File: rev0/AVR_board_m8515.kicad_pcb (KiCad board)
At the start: 2 copper layers, 16 parts, among them IC1 ATMEGA8515-A, IC2 ATMEGA8515-M, K1 SERIAL, P2 LEFT_HEADER, P3 CONN_3X2, P4 RIGHT_HEADER, SW1 SW_PUSH, X1 CRYSTAL_TH, X2 CRYSTAL_SMD

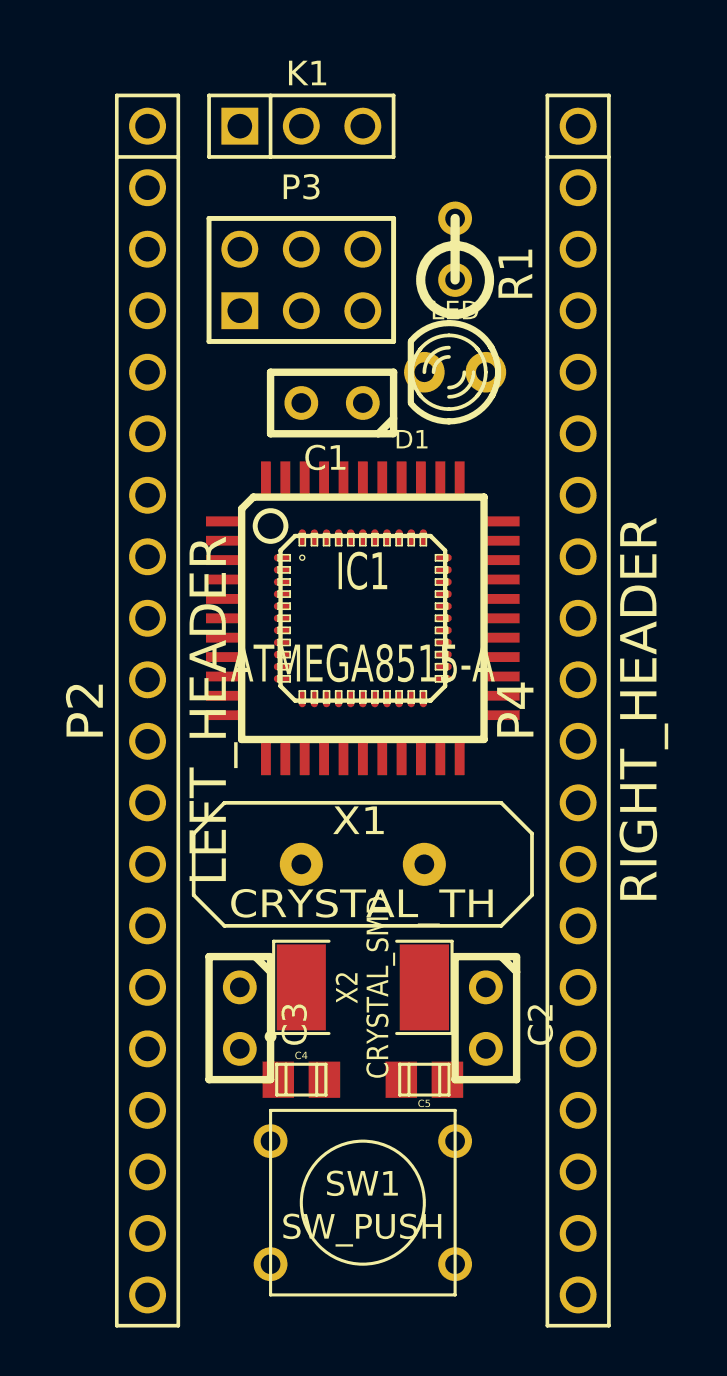
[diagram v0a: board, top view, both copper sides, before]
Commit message: added logo mod file, also added silkscreen refs
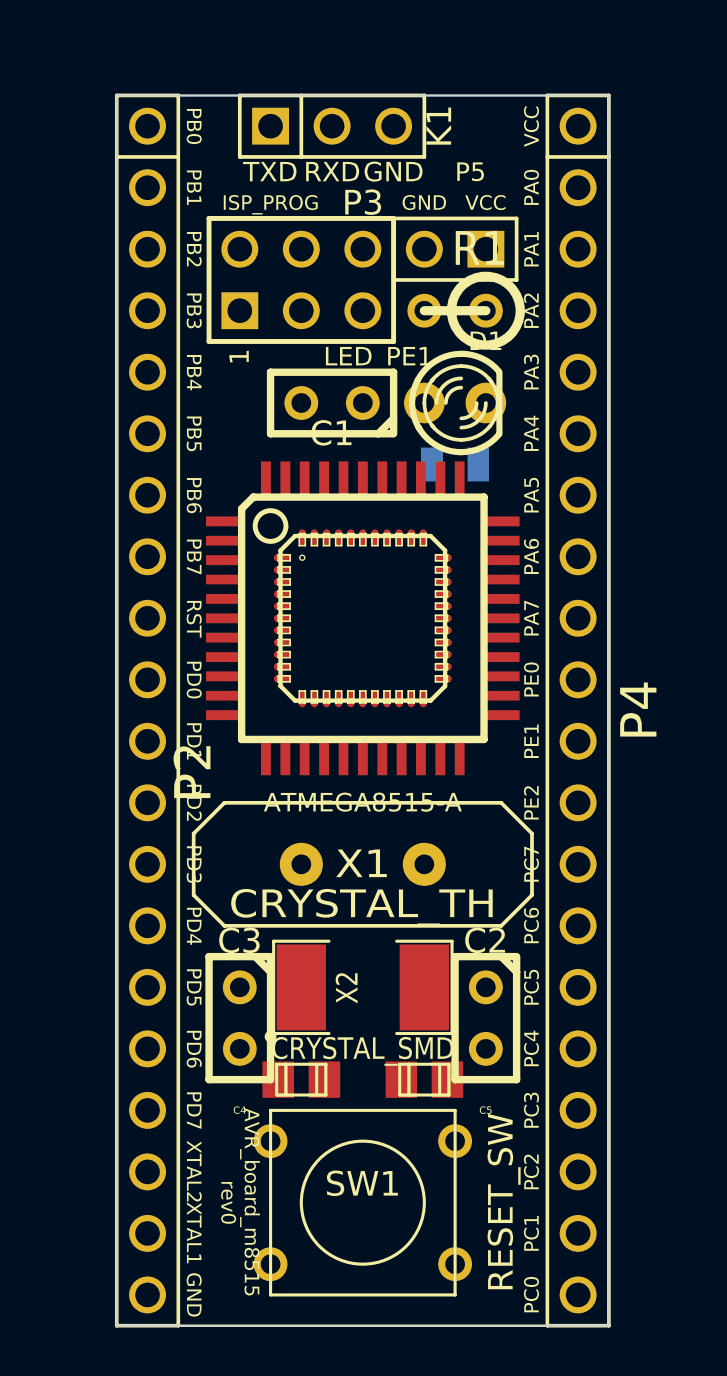
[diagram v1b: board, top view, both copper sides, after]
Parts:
- added G***: LOGO, LOGO, B.Cu at (146.1, 90.2)
- added JP1: LED_JUMPER, SM0805, B.Cu at (149.9, 83.8)
- added P5: EXT_PWR, PIN_ARRAY_2X1, F.Cu at (149.9, 74.9)
- D1: value LED -> LED_PE1
- SW1: value SW_PUSH -> RESET_SW
- moved R1 2.54 mm to (149.9, 77.5), turned to 180 degrees
- moved K1 1.27 mm to (144.8, 69.8)
- moved D1 1.27 mm to (149.9, 81.3), turned to 0 degrees
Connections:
- D1 pad 1: PE1 -> N-0000044
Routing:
- added copper zone on B.Cu, net GND
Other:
- board outline added: 20.3 x 50.8 mm
- board text added: "1"
- board text added: "AVR_board_m8515 rev0"
- board text added: "GND"
- board text added: "ISP_PROG"
- board text added: "PA0"
- board text added: "PA1"
- board text added: "PA2"
- board text added: "PA3"
- board text added: "PA4"
- board text added: "PA5"
- board text added: "PA6"
- board text added: "PA7"
- board text added: "PB0"
- board text added: "PB1"
- board text added: "PB2"
- board text added: "PB3"
- board text added: "PB4"
- board text added: "PB5"
- board text added: "PB6"
- board text added: "PB7"
- board text added: "PC0"
- board text added: "PC1"
- board text added: "PC2"
- board text added: "PC3"
- board text added: "PC4"
- board text added: "PC5"
- board text added: "PC6"
- board text added: "PC7"
- board text added: "PD0"
- board text added: "PD1"
- board text added: "PD2"
- board text added: "PD3"
- board text added: "PD4"
- board text added: "PD5"
- board text added: "PD6"
- board text added: "PD7"
- board text added: "PE0"
- board text added: "PE1"
- board text added: "PE2"
- board text added: "RST"
- board text added: "RXD"
- board text added: "TXD"
- board text added: "VCC"
- board text added: "XTAL1"
- board text added: "XTAL2"

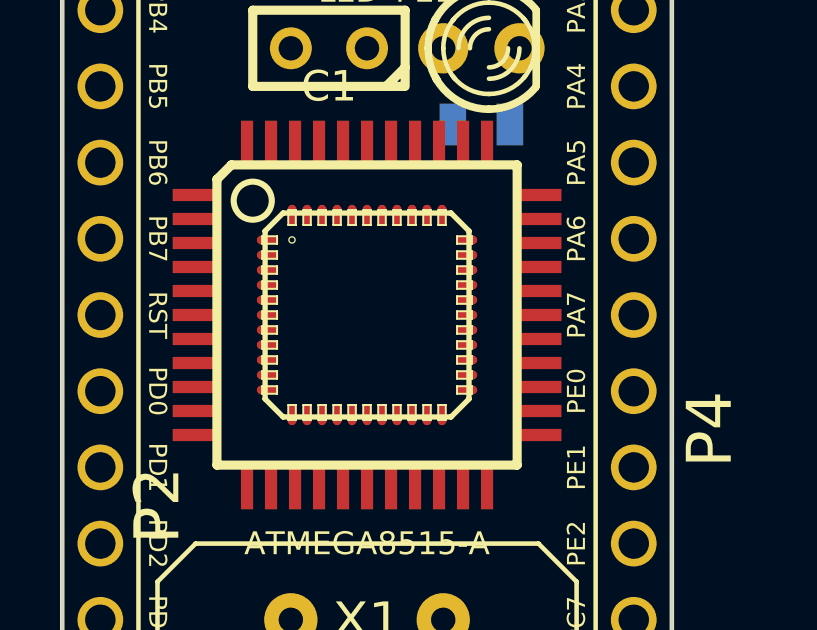
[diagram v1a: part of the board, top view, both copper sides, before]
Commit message: removed the mlf44 footprint due to routing issues
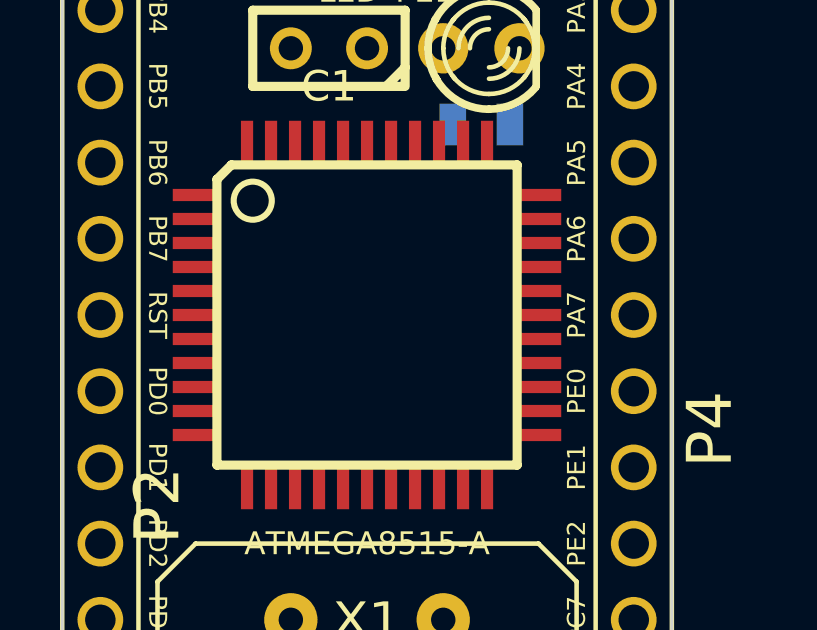
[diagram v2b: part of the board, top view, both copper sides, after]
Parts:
- removed IC2: ATMEGA8515-M, atmel-MLF44

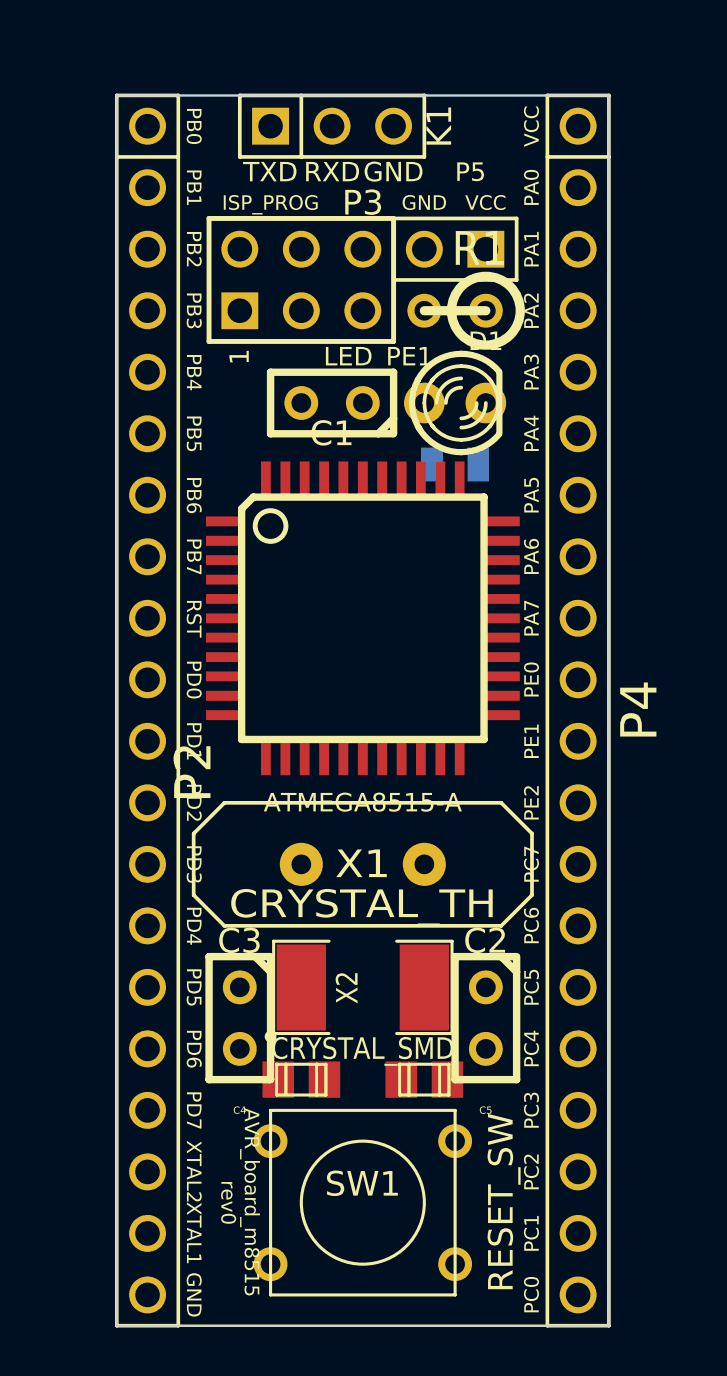
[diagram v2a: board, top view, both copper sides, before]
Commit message: made ses file after using FreeRouting program to route traces
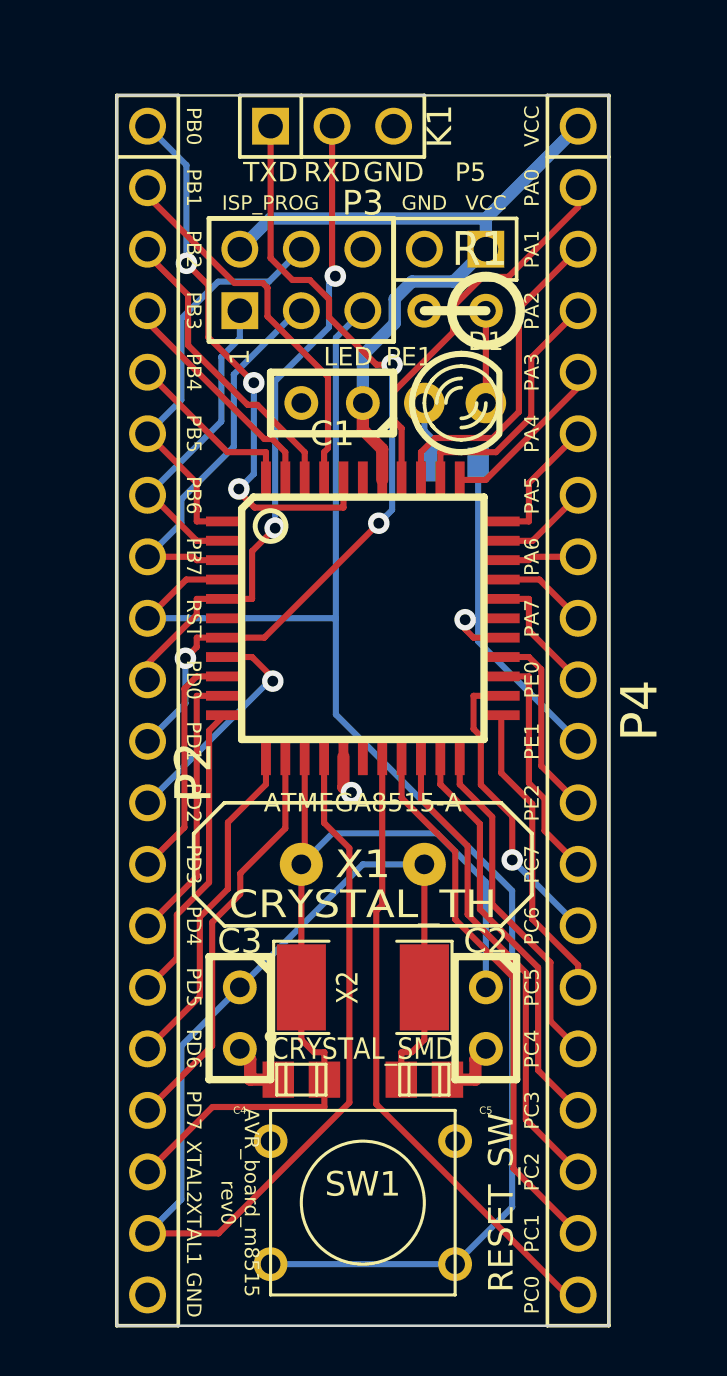
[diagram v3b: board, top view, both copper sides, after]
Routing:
- net RESET: track 0.00 -> 63.1 mm
- net XTAL1: track 0.00 -> 56.3 mm
- net XTAL2: track 0.00 -> 36.9 mm
- net PD1: track 0.00 -> 34.1 mm, vias 0 -> 3
- net VCC: track 0.00 -> 30.3 mm
- net PD0: track 0.00 -> 27.5 mm, vias 0 -> 2
- net PC0: track 0.00 -> 26.0 mm
- net PB0: track 0.00 -> 22.9 mm, vias 0 -> 3
- net PC1: track 0.00 -> 22.7 mm
- net PC2: track 0.00 -> 19.8 mm
- net PB5: track 0.00 -> 17.1 mm
- net PD7: track 0.00 -> 17.0 mm
- net PC3: track 0.00 -> 17.0 mm
- net PB7: track 0.00 -> 16.1 mm
- net PA0: track 0.00 -> 16.0 mm
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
